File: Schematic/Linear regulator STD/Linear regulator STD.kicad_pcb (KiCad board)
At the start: 2 copper layers, 15.2 x 37.3 mm, 10 parts, among them J1 Screw_Terminal_01x04, U1 LM317T

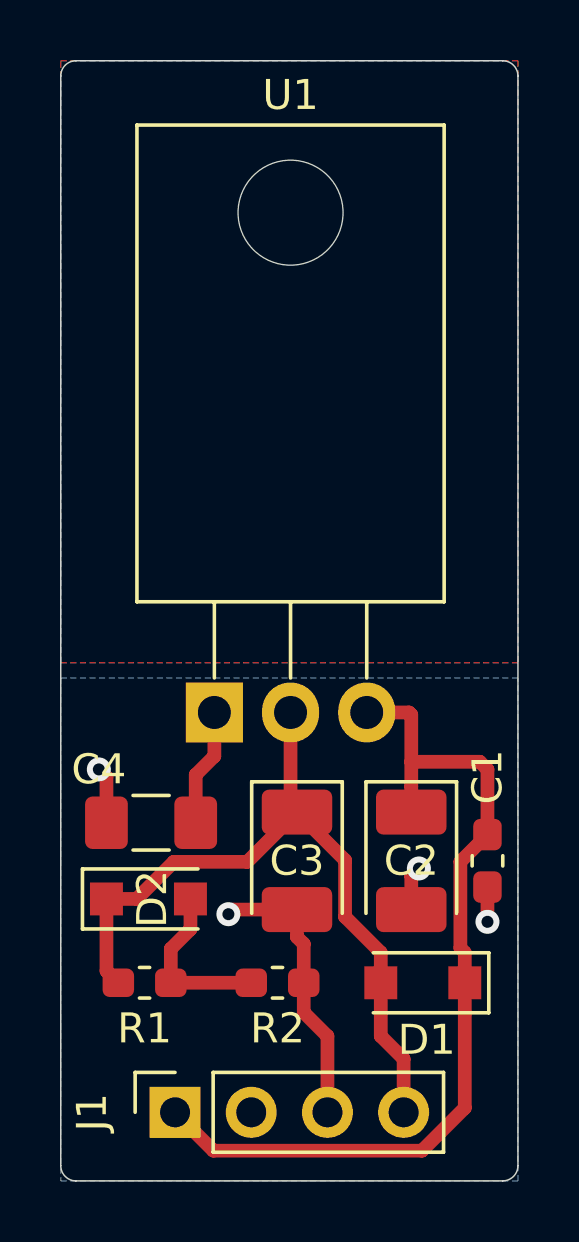
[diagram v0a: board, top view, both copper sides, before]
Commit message: pin header 90 degree update
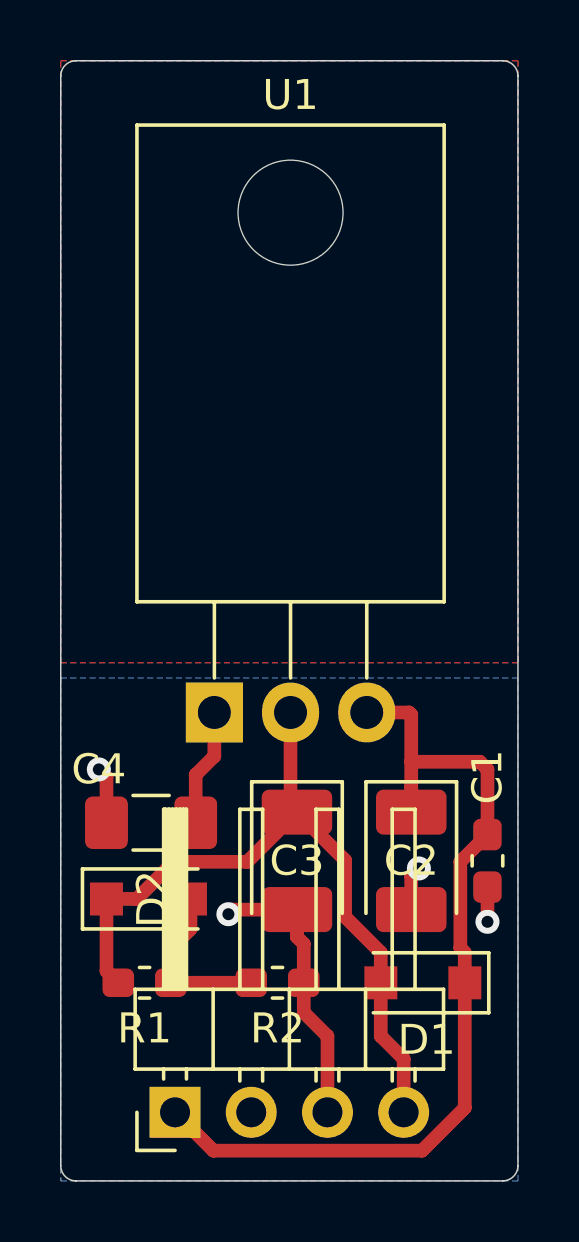
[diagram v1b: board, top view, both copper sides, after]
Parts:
- J1: footprint Connector_PinSocket_2.54mm:PinSocket_1x04_P2.54mm_Vertical -> Connector_PinHeader_2.54mm:PinHeader_1x04_P2.54mm_Horizontal
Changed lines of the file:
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@@
     (add_net "Net-(C4-Pad1)")
   )
-  (module Connector_PinSocket_2.54mm:PinSocket_1x04_P2.54mm_Vertical (layer F.Cu)
+  (module Connector_PinHeader_2.54mm:PinHeader_1x04_P2.54mm_Horizontal (layer F.Cu)
     (at 135.89 95.758 90)
-    (descr "Through hole straight socket strip, 1x04, 2.54mm pitch, single row (from Kicad 4.0.7), script generated")
-    (tags "Through hole socket strip THT 1x04 2.54mm single row")
-    (fp_text reference J1 (at 0 -2.77 90) (layer F.SilkS)
+    (descr "Through hole angled pin header, 1x04, 2.54mm pitch, 6mm pin length, single row")
+    (tags "Through hole angled pin header THT 1x04 2.54mm single row")
+    (fp_text reference J1 (at 4.385 -2.27 90) (layer F.SilkS) hide
       (effects (font (size 1 1) (thickness 0.15)))
     )
-    (fp_text value Screw_Terminal_01x04 (at -3.556 4.318 180) (layer F.Fab)
+    (fp_text value Screw_Terminal_01x04 (at 4.385 9.89 90) (layer F.Fab) hide
       (effects (font (size 1 1) (thickness 0.15)))
     )
-    (fp_text user %R (at 0 3.81) (layer F.Fab)
+    (fp_text user %R (at 2.77 3.81 180) (layer F.Fab) hide
       (effects (font (size 1 1) (thickness 0.15)))
     )
-    (fp_line (start -1.8 9.4) (end -1.8 -1.8) (layer F.CrtYd) (width 0.05))
-    (fp_line (start 1.75 9.4) (end -1.8 9.4) (layer F.CrtYd) (width 0.05))
-    (fp_line (start 1.75 -1.8) (end 1.75 9.4) (layer F.CrtYd) (width 0.05))
-    (fp_line (start -1.8 -1.8) (end 1.75 -1.8) (layer F.CrtYd) (width 0.05))
-    (fp_line (start 0 -1.33) (end 1.33 -1.33) (layer F.SilkS) (width 0.12))
-    (fp_line (start 1.33 -1.33) (end 1.33 0) (layer F.SilkS) (width 0.12))
-    (fp_line (start 1.33 1.27) (end 1.33 8.95) (layer F.SilkS) (width 0.12))
-    (fp_line (start -1.33 8.95) (end 1.33 8.95) (layer F.SilkS) (width 0.12))
-    (fp_line (start -1.33 1.27) (end -1.33 8.95) (layer F.SilkS) (width 0.12))
-    (fp_line (start -1.33 1.27) (end 1.33 1.27) (layer F.SilkS) (width 0.12))
-    (fp_line (start -1.27 8.89) (end -1.27 -1.27) (layer F.Fab) (width 0.1))
-    (fp_line (start 1.27 8.89) (end -1.27 8.89) (layer F.Fab) (width 0.1))
-    (fp_line (start 1.27 -0.635) (end 1.27 8.89) (layer F.Fab) (width 0.1))
-    (fp_line (start 0.635 -1.27) (end 1.27 -0.635) (layer F.Fab) (width 0.1))
-    (fp_line (start -1.27 -1.27) (end 0.635 -1.27) (layer F.Fab) (width 0.1))
+    (fp_line (start 10.55 -1.8) (end -1.8 -1.8) (layer F.CrtYd) (width 0.05))
+    (fp_line (start 10.55 9.4) (end 10.55 -1.8) (layer F.CrtYd) (width 0.05))
+    (fp_line (start -1.8 9.4) (end 10.55 9.4) (layer F.CrtYd) (width 0.05))
+    (fp_line (start -1.8 -1.8) (end -1.8 9.4) (layer F.CrtYd) (width 0.05))
+    (fp_line (start -1.27 -1.27) (end 0 -1.27) (layer F.SilkS) (width 0.12))
+    (fp_line (start -1.27 0) (end -1.27 -1.27) (layer F.SilkS) (width 0.12))
+    (fp_line (start 1.042929 8) (end 1.44 8) (layer F.SilkS) (width 0.12))
+    (fp_line (start 1.042929 7.24) (end 1.44 7.24) (layer F.SilkS) (width 0.12))
+    (fp_line (start 10.1 8) (end 4.1 8) (layer F.SilkS) (width 0.12))
+    (fp_line (start 10.1 7.24) (end 10.1 8) (layer F.SilkS) (width 0.12))
+    (fp_line (start 4.1 7.24) (end 10.1 7.24) (layer F.SilkS) (width 0.12))
+    (fp_line (start 1.44 6.35) (end 4.1 6.35) (layer F.SilkS) (width 0.12))
+    (fp_line (start 1.042929 5.46) (end 1.44 5.46) (layer F.SilkS) (width 0.12))
+    (fp_line (start 1.042929 4.7) (end 1.44 4.7) (layer F.SilkS) (width 0.12))
+    (fp_line (start 10.1 5.46) (end 4.1 5.46) (layer F.SilkS) (width 0.12))
+    (fp_line (start 10.1 4.7) (end 10.1 5.46) (layer F.SilkS) (width 0.12))
+    (fp_line (start 4.1 4.7) (end 10.1 4.7) (layer F.SilkS) (width 0.12))
+    (fp_line (start 1.44 3.81) (end 4.1 3.81) (layer F.SilkS) (width 0.12))
+    (fp_line (start 1.042929 2.92) (end 1.44 2.92) (layer F.SilkS) (width 0.12))
+    (fp_line (start 1.042929 2.16) (end 1.44 2.16) (layer F.SilkS) (width 0.12))
+    (fp_line (start 10.1 2.92) (end 4.1 2.92) (layer F.SilkS) (width 0.12))
+    (fp_line (start 10.1 2.16) (end 10.1 2.92) (layer F.SilkS) (width 0.12))
+    (fp_line (start 4.1 2.16) (end 10.1 2.16) (layer F.SilkS) (width 0.12))
+    (fp_line (start 1.44 1.27) (end 4.1 1.27) (layer F.SilkS) (width 0.12))
+    (fp_line (start 1.11 0.38) (end 1.44 0.38) (layer F.SilkS) (width 0.12))
+    (fp_line (start 1.11 -0.38) (end 1.44 -0.38) (layer F.SilkS) (width 0.12))
+    (fp_line (start 4.1 0.28) (end 10.1 0.28) (layer F.SilkS) (width 0.12))
+    (fp_line (start 4.1 0.16) (end 10.1 0.16) (layer F.SilkS) (width 0.12))
+    (fp_line (start 4.1 0.04) (end 10.1 0.04) (layer F.SilkS) (width 0.12))
+    (fp_line (start 4.1 -0.08) (end 10.1 -0.08) (layer F.SilkS) (width 0.12))
+    (fp_line (start 4.1 -0.2) (end 10.1 -0.2) (layer F.SilkS) (width 0.12))
+    (fp_line (start 4.1 -0.32) (end 10.1 -0.32) (layer F.SilkS) (width 0.12))
+    (fp_line (start 10.1 0.38) (end 4.1 0.38) (layer F.SilkS) (width 0.12))
+    (fp_line (start 10.1 -0.38) (end 10.1 0.38) (layer F.SilkS) (width 0.12))
+    (fp_line (start 4.1 -0.38) (end 10.1 -0.38) (layer F.SilkS) (width 0.12))
+    (fp_line (start 4.1 -1.33) (end 1.44 -1.33) (layer F.SilkS) (width 0.12))
+    (fp_line (start 4.1 8.95) (end 4.1 -1.33) (layer F.SilkS) (width 0.12))
+    (fp_line (start 1.44 8.95) (end 4.1 8.95) (layer F.SilkS) (width 0.12))
+    (fp_line (start 1.44 -1.33) (end 1.44 8.95) (layer F.SilkS) (width 0.12))
+    (fp_line (start 4.04 7.94) (end 10.04 7.94) (layer F.Fab) (width 0.1))
+    (fp_line (start 10.04 7.3) (end 10.04 7.94) (layer F.Fab) (width 0.1))
+    (fp_line (start 4.04 7.3) (end 10.04 7.3) (layer F.Fab) (width 0.1))
+    (fp_line (start -0.32 7.94) (end 1.5 7.94) (layer F.Fab) (width 0.1))
+    (fp_line (start -0.32 7.3) (end -0.32 7.94) (layer F.Fab) (width 0.1))
+    (fp_line (start -0.32 7.3) (end 1.5 7.3) (layer F.Fab) (width 0.1))
+    (fp_line (start 4.04 5.4) (end 10.04 5.4) (layer F.Fab) (width 0.1))
+    (fp_line (start 10.04 4.76) (end 10.04 5.4) (layer F.Fab) (width 0.1))
+    (fp_line (start 4.04 4.76) (end 10.04 4.76) (layer F.Fab) (width 0.1))
+    (fp_line (start -0.32 5.4) (end 1.5 5.4) (layer F.Fab) (width 0.1))
+    (fp_line (start -0.32 4.76) (end -0.32 5.4) (layer F.Fab) (width 0.1))
+    (fp_line (start -0.32 4.76) (end 1.5 4.76) (layer F.Fab) (width 0.1))
+    (fp_line (start 4.04 2.86) (end 10.04 2.86) (layer F.Fab) (width 0.1))
+    (fp_line (start 10.04 2.22) (end 10.04 2.86) (layer F.Fab) (width 0.1))
+    (fp_line (start 4.04 2.22) (end 10.04 2.22) (layer F.Fab) (width 0.1))
+    (fp_line (start -0.32 2.86) (end 1.5 2.86) (layer F.Fab) (width 0.1))
+    (fp_line (start -0.32 2.22) (end -0.32 2.86) (layer F.Fab) (width 0.1))
+    (fp_line (start -0.32 2.22) (end 1.5 2.22) (layer F.Fab) (width 0.1))
+    (fp_line (start 4.04 0.32) (end 10.04 0.32) (layer F.Fab) (width 0.1))
+    (fp_line (start 10.04 -0.32) (end 10.04 0.32) (layer F.Fab) (width 0.1))
+    (fp_line (start 4.04 -0.32) (end 10.04 -0.32) (layer F.Fab) (width 0.1))
+    (fp_line (start -0.32 0.32) (end 1.5 0.32) (layer F.Fab) (width 0.1))
+    (fp_line (start -0.32 -0.32) (end -0.32 0.32) (layer F.Fab) (width 0.1))
+    (fp_line (start -0.32 -0.32) (end 1.5 -0.32) (layer F.Fab) (width 0.1))
+    (fp_line (start 1.5 -0.635) (end 2.135 -1.27) (layer F.Fab) (width 0.1))
+    (fp_line (start 1.5 8.89) (end 1.5 -0.635) (layer F.Fab) (width 0.1))
+    (fp_line (start 4.04 8.89) (end 1.5 8.89) (layer F.Fab) (width 0.1))
+    (fp_line (start 4.04 -1.27) (end 4.04 8.89) (layer F.Fab) (width 0.1))
+    (fp_line (start 2.135 -1.27) (end 4.04 -1.27) (layer F.Fab) (width 0.1))
     (pad 4 thru_hole oval (at 0 7.62 90) (size 1.7 1.7) (drill 1) (layers *.Cu *.Mask)
       (net 2 /VOUT))
@@
     (pad 1 thru_hole rect (at 0 0 90) (size 1.7 1.7) (drill 1) (layers *.Cu *.Mask)
       (net 4 /VIN))
-    (model ${KISYS3DMOD}/Connector_PinSocket_2.54mm.3dshapes/PinSocket_1x04_P2.54mm_Vertical.wrl
-      (at (xyz 0 0 0))
+    (model ${KISYS3DMOD}/Connector_PinHeader_2.54mm.3dshapes/PinHeader_1x04_P2.54mm_Horizontal.wrl
+      (offset (xyz 0 -7.5 0))
       (scale (xyz 1 1 1))
-      (rotate (xyz 0 0 0))
+      (rotate (xyz 0 0 180))
     )
   )

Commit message: added LED, silkscreen fix
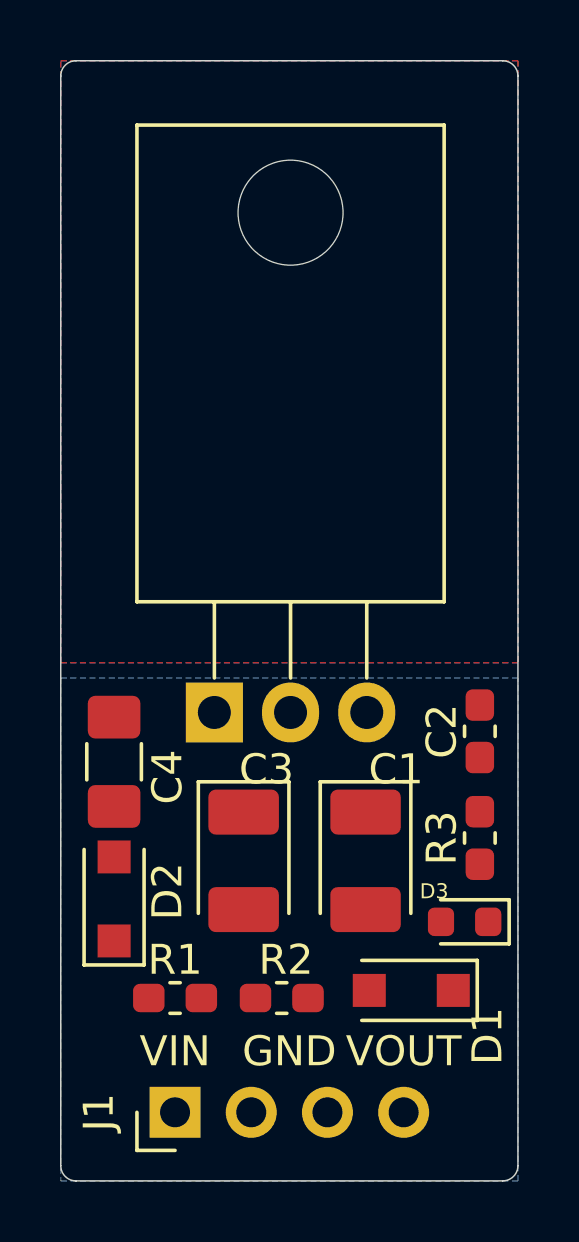
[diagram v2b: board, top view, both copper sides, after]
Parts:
- added D3: LG_L29K-G2J1-24-Z, LED_SMD:LED_0603_1608Metric, F.Cu at (145.5, 89.4)
- added R3: 560, Resistor_SMD:R_0603_1608Metric_Pad1.05x0.95mm_HandSolder, F.Cu at (146.1, 86.6)
- added REF**: OSHW-Logo2_9.8x8mm_SilkScreen, Symbol:OSHW-Logo2_9.8x8mm_SilkScreen, B.Cu at (139.7, 72.4)
- J1: footprint Connector_PinHeader_2.54mm:PinHeader_1x04_P2.54mm_Horizontal -> Connector_PinHeader_2.54mm_OSHW:PinHeader_1x04_P2.54mm_Horizontal
- moved C2 4.33 mm to (146.1, 83.1)
- moved C4 2.38 mm to (133.9, 84.1), turned to 270 degrees
- moved C3 1.78 mm to (138.2, 87.4)
- moved C1 1.52 mm to (142.2, 87.4)
- moved D2 1.15 mm to (133.9, 88.6), turned to 90 degrees
- moved R1 1.14 mm to (135.9, 91.9)
- moved R2 0.53 mm to (139.4, 91.9)
- moved D1 0.46 mm to (143.8, 91.7)
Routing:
- net /VIN: track 29.9 -> 0.00 mm
- net /VOUT: track 25.4 -> 0.00 mm
- net GND: track 14.0 -> 0.00 mm, vias 4 -> 0
- net Net-(C4-Pad1): track 9.93 -> 0.00 mm
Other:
- board text added: "GND"
- board text added: "VIN"
- board text added: "VOUT"

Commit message: partial route
work in progress
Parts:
- moved D3 3.56 mm to (145.5, 85.9)
- moved R3 1.97 mm to (146.3, 88.6)
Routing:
- net /VOUT: track 0.00 -> 31.7 mm
- net /VIN: track 0.00 -> 15.0 mm
- net Net-(C4-Pad1): track 0.00 -> 14.4 mm
- net GND: track 0.00 -> 7.02 mm
- net Net-(D3-Pad1): track 0.00 -> 1.84 mm
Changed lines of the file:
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@@
     (thickness 1.6)
     (drawings 12)
-    (tracks 0)
+    (tracks 45)
     (zones 0)
     (modules 13)
@@
   (page A4)
   (layers
-    (0 F.Cu signal hide)
-    (31 B.Cu signal hide)
-    (32 B.Adhes user hide)
-    (33 F.Adhes user hide)
-    (34 B.Paste user hide)
-    (35 F.Paste user hide)
+    (0 F.Cu signal)
+    (31 B.Cu signal)
+    (32 B.Adhes user)
+    (33 F.Adhes user)
+    (34 B.Paste user)
+    (35 F.Paste user)
     (36 B.SilkS user)
     (37 F.SilkS user)
     (38 B.Mask user)
-    (39 F.Mask user hide)
+    (39 F.Mask user)
     (40 Dwgs.User user)
     (41 Cmts.User user)
@@
   )
   (setup
-    (last_trace_width 0.25)
+    (last_trace_width 0.3048)
     (user_trace_width 0.3048)
     (user_trace_width 0.4572)
+    (user_trace_width 0.8)
     (trace_clearance 0.2)
     (zone_clearance 0.508)
@@
     (via_min_size 0.4)
     (via_min_drill 0.3)
+    (user_via 0.7 0.5)
     (uvia_size 0.3)
     (uvia_drill 0.1)
@@
   )
   (module LED_SMD:LED_0603_1608Metric (layer F.Cu)
-    (at 145.542 89.408 180)
+    (at 145.4658 85.852 180)
     (descr "LED SMD 0603 (1608 Metric), square (rectangular) end terminal, IPC_7351 nominal, (Body size source: http://www.tortai-tech.com/upload/download/2011102023233369053.pdf), generated with kicad-footprint-generator")
     (tags diode)
@@
   )
   (module Resistor_SMD:R_0603_1608Metric_Pad1.05x0.95mm_HandSolder (layer F.Cu)
-    (at 146.05 86.614 90)
+    (at 146.2532 88.5698 90)
     (descr "Resistor SMD 0603 (1608 Metric), square (rectangular) end terminal, IPC_7351 nominal with elongated pad for handsoldering. (Body size source: http://www.tortai-tech.com/upload/download/2011102023233369053.pdf), generated with kicad-footprint-generator")
     (tags "resistor handsolder")
@@
   (gr_arc (start 132.588 61.214) (end 132.588 60.706) (angle -90) (layer Edge.Cuts) (width 0.05))
   (gr_poly (pts (xy 132.588 61.214) (xy 146.812 61.214) (xy 146.812 80.772) (xy 132.588 80.772)) (layer F.Mask) (width 0.1))
+  (segment (start 144.6783 84.5059) (end 144.6783 85.852) (width 0.3048) (layer F.Cu) (net 1))
+  (segment (start 146.05 83.933) (end 145.2512 83.933) (width 0.3048) (layer F.Cu) (net 1))
+  (segment (start 145.2512 83.933) (end 144.6783 84.5059) (width 0.3048) (layer F.Cu) (net 1))
+  (segment (start 138.176 89.001) (end 142.24 89.001) (width 0.8) (layer F.Cu) (net 1))
+  (segment (start 142.364 91.694) (end 142.364 92.7578) (width 0.4572) (layer F.Cu) (net 2))
+  (segment (start 143.51 93.9038) (end 143.51 95.758) (width 0.4572) (layer F.Cu) (net 2))
+  (segment (start 142.364 92.7578) (end 143.51 93.9038) (width 0.4572) (layer F.Cu) (net 2))
+  (segment (start 145.3642 93.9038) (end 143.51 93.9038) (width 0.3048) (layer F.Cu) (net 2))
+  (segment (start 146.2532 93.0148) (end 145.3642 93.9038) (width 0.3048) (layer F.Cu) (net 2))
+  (segment (start 146.2532 89.4448) (end 146.2532 93.0148) (width 0.3048) (layer F.Cu) (net 2))
+  (segment (start 139.74 84.187) (end 138.176 85.751) (width 0.8) (layer F.Cu) (net 2))
+  (segment (start 139.74 82.43) (end 139.74 84.187) (width 0.8) (layer F.Cu) (net 2))
+  (segment (start 141.71439 91.04439) (end 142.364 91.694) (width 0.4572) (layer F.Cu) (net 2))
+  (segment (start 137.834688 91.04439) (end 141.71439 91.04439) (width 0.4572) (layer F.Cu) (net 2))
+  (segment (start 136.57239 89.782092) (end 137.834688 91.04439) (width 0.4572) (layer F.Cu) (net 2))
+  (segment (start 136.57239 88.219908) (end 136.57239 89.782092) (width 0.4572) (layer F.Cu) (net 2))
+  (segment (start 138.176 86.616298) (end 136.57239 88.219908) (width 0.4572) (layer F.Cu) (net 2))
+  (segment (start 138.176 85.751) (end 138.176 86.616298) (width 0.4572) (layer F.Cu) (net 2))
+  (segment (start 133.858 90.791) (end 135.015 91.948) (width 0.3048) (layer F.Cu) (net 2))
+  (segment (start 133.858 90.046) (end 133.858 90.791) (width 0.3048) (layer F.Cu) (net 2))
+  (segment (start 135.514072 90.84041) (end 136.57239 89.782092) (width 0.3048) (layer F.Cu) (net 2))
+  (segment (start 135.514072 91.448928) (end 135.514072 90.84041) (width 0.3048) (layer F.Cu) (net 2))
+  (segment (start 135.015 91.948) (end 135.514072 91.448928) (width 0.3048) (layer F.Cu) (net 2))
+  (segment (start 133.858 88.1008) (end 133.858 87.246) (width 0.3048) (layer F.Cu) (net 3))
+  (segment (start 132.955599 89.003201) (end 133.858 88.1008) (width 0.3048) (layer F.Cu) (net 3))
+  (segment (start 132.955599 91.247859) (end 132.955599 89.003201) (width 0.3048) (layer F.Cu) (net 3))
+  (segment (start 134.48315 92.77541) (end 132.955599 91.247859) (width 0.3048) (layer F.Cu) (net 3))
+  (segment (start 135.93759 92.77541) (end 134.48315 92.77541) (width 0.3048) (layer F.Cu) (net 3))
+  (segment (start 136.765 91.948) (end 135.93759 92.77541) (width 0.3048) (layer F.Cu) (net 3))
+  (segment (start 138.571 91.948) (end 136.765 91.948) (width 0.3048) (layer F.Cu) (net 3))
+  (segment (start 135.9427 82.43) (end 137.2 82.43) (width 0.3048) (layer F.Cu) (net 3))
+  (segment (start 133.858 82.5865) (end 135.7862 82.5865) (width 0.3048) (layer F.Cu) (net 3))
+  (segment (start 135.7862 82.5865) (end 135.9427 82.43) (width 0.3048) (layer F.Cu) (net 3))
+  (segment (start 142.28 85.711) (end 142.24 85.751) (width 0.8) (layer F.Cu) (net 4))
+  (segment (start 142.28 82.43) (end 142.28 85.711) (width 0.8) (layer F.Cu) (net 4))
+  (segment (start 144.1568 91.694) (end 145.164 91.694) (width 0.4572) (layer F.Cu) (net 4))
+  (segment (start 142.24 86.616298) (end 142.24 85.751) (width 0.4572) (layer F.Cu) (net 4))
+  (segment (start 143.84361 88.219908) (end 142.24 86.616298) (width 0.4572) (layer F.Cu) (net 4))
+  (segment (start 144.1568 91.694) (end 143.84361 91.38081) (width 0.4572) (layer F.Cu) (net 4))
+  (segment (start 143.84361 91.38081) (end 143.84361 88.219908) (width 0.4572) (layer F.Cu) (net 4))
+  (segment (start 142.28 82.43) (end 144.2904 82.43) (width 0.3048) (layer F.Cu) (net 4))
+  (segment (start 144.5374 82.183) (end 146.05 82.183) (width 0.3048) (layer F.Cu) (net 4))
+  (segment (start 144.2904 82.43) (end 144.5374 82.183) (width 0.3048) (layer F.Cu) (net 4))
+  (segment (start 146.2533 87.6947) (end 146.2532 87.6948) (width 0.3048) (layer F.Cu) (net 5))
+  (segment (start 146.2533 85.852) (end 146.2533 87.6947) (width 0.3048) (layer F.Cu) (net 5))
   (zone (net 0) (net_name "") (layer B.Cu) (hatch edge 0.508)
     (connect_pads (clearance 0.508))
